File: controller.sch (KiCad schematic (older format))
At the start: 12 parts

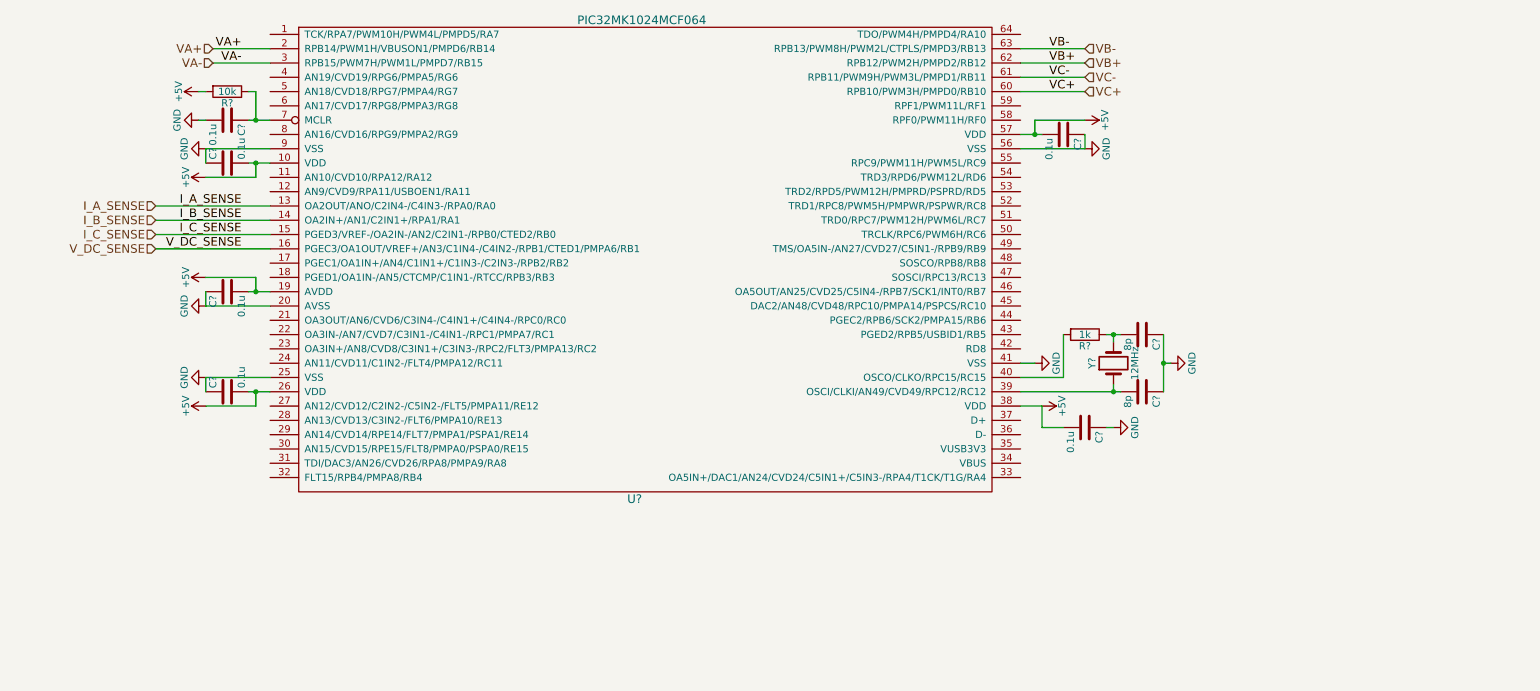
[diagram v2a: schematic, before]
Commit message: Implementing more faults and organizing.
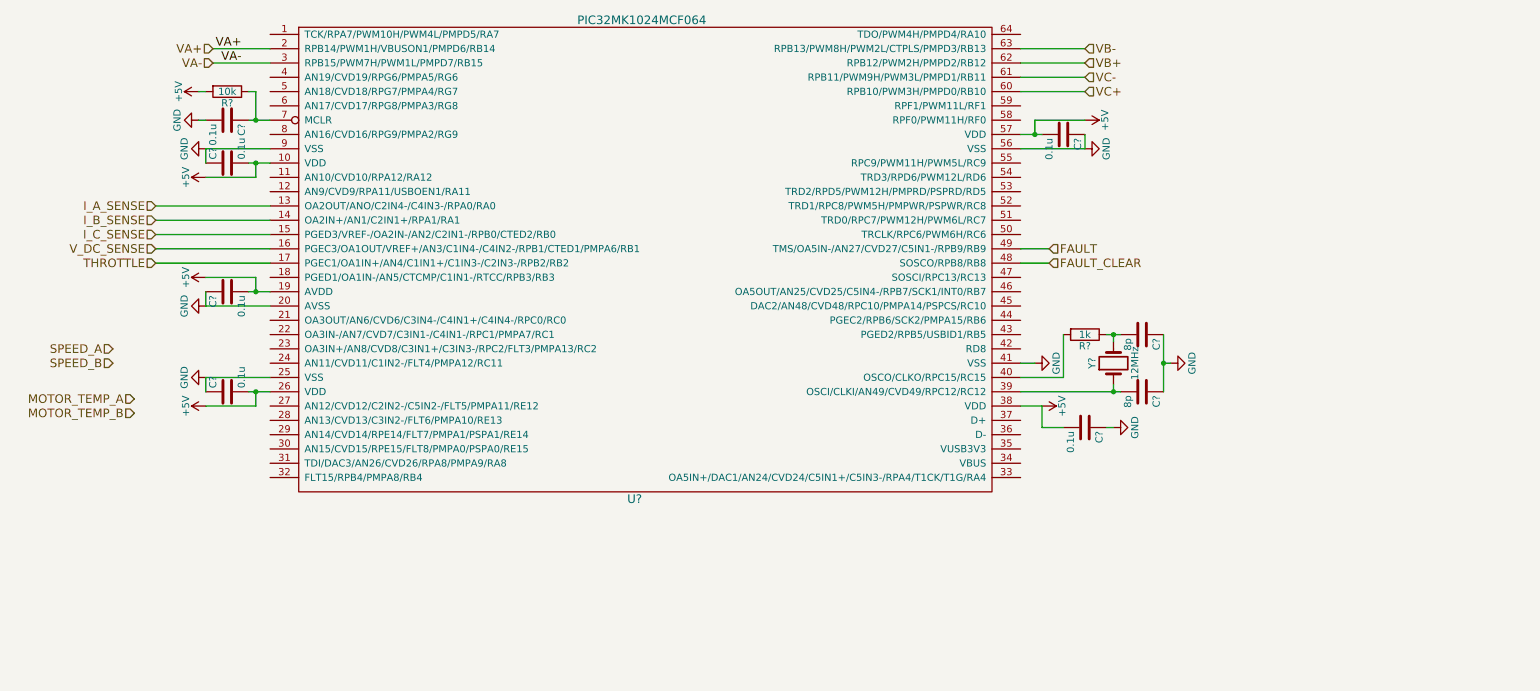
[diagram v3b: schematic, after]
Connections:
- net THROTTLE: now reaches U?.17 (PGEC1/OA1IN+/AN4/C1IN1+/C1IN3-/C2IN3-/RPB2/RB2)
- net FAULT_CLEAR: now reaches U?.48 (SOSCO/RPB8/RB8)
- net FAULT: now reaches U?.49 (TMS/OA5IN-/AN27/CVD27/C5IN1-/RPB9/RB9)
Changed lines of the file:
@@
 $Descr A4 11693 8268
 encoding utf-8
-Sheet 2 9
+Sheet 2 15
 Title ""
 Date ""
@@
 $EndComp
 $Comp
-L GND #PWR?
+L GND #PWR01
 U 1 1 5AEC2707
 P 8600 3350
-F 0 "#PWR?" H 8600 3100 50  0001 C CNN
+F 0 "#PWR01" H 8600 3100 50  0001 C CNN
 F 1 "GND" H 8600 3200 50  0000 C CNN
 F 2 "" H 8600 3350 50  0001 C CNN
@@
 $EndComp
 $Comp
-L GND #PWR?
+L GND #PWR02
 U 1 1 5AEC270D
 P 1850 1850
-F 0 "#PWR?" H 1850 1600 50  0001 C CNN
+F 0 "#PWR02" H 1850 1600 50  0001 C CNN
 F 1 "GND" H 1850 1700 50  0000 C CNN
 F 2 "" H 1850 1850 50  0001 C CNN
@@
 $EndComp
 $Comp
-L +5V #PWR?
+L +5V #PWR03
 U 1 1 5AEC271A
 P 1850 2050
-F 0 "#PWR?" H 1850 1900 50  0001 C CNN
+F 0 "#PWR03" H 1850 1900 50  0001 C CNN
 F 1 "+5V" H 1850 2190 50  0000 C CNN
 F 2 "" H 1850 2050 50  0001 C CNN
@@
 $EndComp
 $Comp
-L GND #PWR?
+L GND #PWR04
 U 1 1 5AEC2720
 P 1850 3450
-F 0 "#PWR?" H 1850 3200 50  0001 C CNN
+F 0 "#PWR04" H 1850 3200 50  0001 C CNN
 F 1 "GND" H 1850 3300 50  0000 C CNN
 F 2 "" H 1850 3450 50  0001 C CNN
@@
 $EndComp
 $Comp
-L +5V #PWR?
+L +5V #PWR05
 U 1 1 5AEC272D
 P 1850 3650
-F 0 "#PWR?" H 1850 3500 50  0001 C CNN
+F 0 "#PWR05" H 1850 3500 50  0001 C CNN
 F 1 "+5V" H 1850 3790 50  0000 C CNN
 F 2 "" H 1850 3650 50  0001 C CNN
@@
 $EndComp
 $Comp
-L GND #PWR?
+L GND #PWR06
 U 1 1 5AEC2733
 P 8000 1850
-F 0 "#PWR?" H 8000 1600 50  0001 C CNN
+F 0 "#PWR06" H 8000 1600 50  0001 C CNN
 F 1 "GND" H 8000 1700 50  0000 C CNN
 F 2 "" H 8000 1850 50  0001 C CNN
@@
 $EndComp
 $Comp
-L +5V #PWR?
+L +5V #PWR07
 U 1 1 5AEC2740
 P 8000 1650
-F 0 "#PWR?" H 8000 1500 50  0001 C CNN
+F 0 "#PWR07" H 8000 1500 50  0001 C CNN
 F 1 "+5V" H 8000 1790 50  0000 C CNN
 F 2 "" H 8000 1650 50  0001 C CNN
@@
 $EndComp
 $Comp
-L GND #PWR?
+L GND #PWR08
 U 1 1 5AEC2746
 P 1850 2950
-F 0 "#PWR?" H 1850 2700 50  0001 C CNN
+F 0 "#PWR08" H 1850 2700 50  0001 C CNN
 F 1 "GND" H 1850 2800 50  0000 C CNN
 F 2 "" H 1850 2950 50  0001 C CNN
@@
 $EndComp
 $Comp
-L +5V #PWR?
+L +5V #PWR09
 U 1 1 5AEC2753
 P 1850 2750
-F 0 "#PWR?" H 1850 2600 50  0001 C CNN
+F 0 "#PWR09" H 1850 2600 50  0001 C CNN
 F 1 "+5V" H 1850 2890 50  0000 C CNN
 F 2 "" H 1850 2750 50  0001 C CNN
@@
 $EndComp
 $Comp
-L GND #PWR?
+L GND #PWR010
 U 1 1 5AEC2759
 P 7650 3350
-F 0 "#PWR?" H 7650 3100 50  0001 C CNN
+F 0 "#PWR010" H 7650 3100 50  0001 C CNN
 F 1 "GND" H 7650 3200 50  0000 C CNN
 F 2 "" H 7650 3350 50  0001 C CNN
@@
 $EndComp
 $Comp
-L GND #PWR?
+L GND #PWR011
 U 1 1 5AEC275F
 P 8200 3800
-F 0 "#PWR?" H 8200 3550 50  0001 C CNN
+F 0 "#PWR011" H 8200 3550 50  0001 C CNN
 F 1 "GND" H 8200 3650 50  0000 C CNN
 F 2 "" H 8200 3800 50  0001 C CNN
@@
 $EndComp
 $Comp
-L +5V #PWR?
+L +5V #PWR012
 U 1 1 5AEC276C
 P 7700 3650
-F 0 "#PWR?" H 7700 3500 50  0001 C CNN
+F 0 "#PWR012" H 7700 3500 50  0001 C CNN
 F 1 "+5V" H 7700 3790 50  0000 C CNN
 F 2 "" H 7700 3650 50  0001 C CNN
@@
 $EndComp
 $Comp
-L GND #PWR?
+L GND #PWR013
 U 1 1 5AEC2780
 P 1800 1650
-F 0 "#PWR?" H 1800 1400 50  0001 C CNN
+F 0 "#PWR013" H 1800 1400 50  0001 C CNN
 F 1 "GND" H 1800 1500 50  0000 C CNN
 F 2 "" H 1800 1650 50  0001 C CNN
@@
 $EndComp
 $Comp
-L +5V #PWR?
+L +5V #PWR014
 U 1 1 5AEC2786
 P 1800 1450
-F 0 "#PWR?" H 1800 1300 50  0001 C CNN
+F 0 "#PWR014" H 1800 1300 50  0001 C CNN
 F 1 "+5V" H 1800 1590 50  0000 C CNN
 F 2 "" H 1800 1450 50  0001 C CNN
@@
 Wire Wire Line
 	1900 1250 2300 1250
-Text Label 7750 1250 0    60   ~ 0
-VB+
-Text Label 7750 1350 0    60   ~ 0
-VC-
-Text Label 7750 1450 0    60   ~ 0
-VC+
 Wire Wire Line
 	7550 1450 8000 1450
@@
 Wire Wire Line
 	7550 1250 8000 1250
-Text Label 7750 1150 0    60   ~ 0
-VB-
 Wire Wire Line
 	7550 1150 8000 1150
-Text Label 2100 2250 2    60   ~ 0
-I_A_SENSE
-Text Label 2100 2350 2    60   ~ 0
-I_B_SENSE
-Text Label 2100 2450 2    60   ~ 0
-I_C_SENSE
 Wire Wire Line
 	1500 2250 2300 2250
@@
 Wire Wire Line
 	1500 2450 2300 2450
-Text Label 2100 2550 2    60   ~ 0
-V_DC_SENSE
 Wire Wire Line
 	1500 2550 2300 2550
@@
 Text HLabel 1500 2550 0    60   Input ~ 0
 V_DC_SENSE
+Text HLabel 1500 2650 0    60   Input ~ 0
+THROTTLE
+Wire Wire Line
+	1500 2650 2300 2650
+Text HLabel 7750 2550 2    60   Input ~ 0
+FAULT
+Wire Wire Line
+	7750 2550 7550 2550
+Text HLabel 7750 2650 2    60   Input ~ 0
+FAULT_CLEAR
+Wire Wire Line
+	7750 2650 7550 2650
+Text HLabel 1200 3250 0    60   Input ~ 0
+SPEED_A
+Text HLabel 1200 3350 0    60   Input ~ 0
+SPEED_B
+Text HLabel 1350 3600 0    60   Input ~ 0
+MOTOR_TEMP_A
+Text HLabel 1350 3700 0    60   Input ~ 0
+MOTOR_TEMP_B
 $EndSCHEMATC

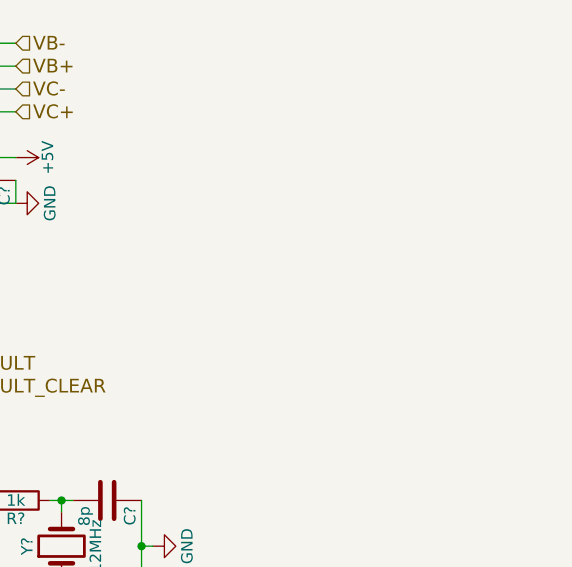
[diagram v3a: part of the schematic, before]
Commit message: Adding contactor placeholders.
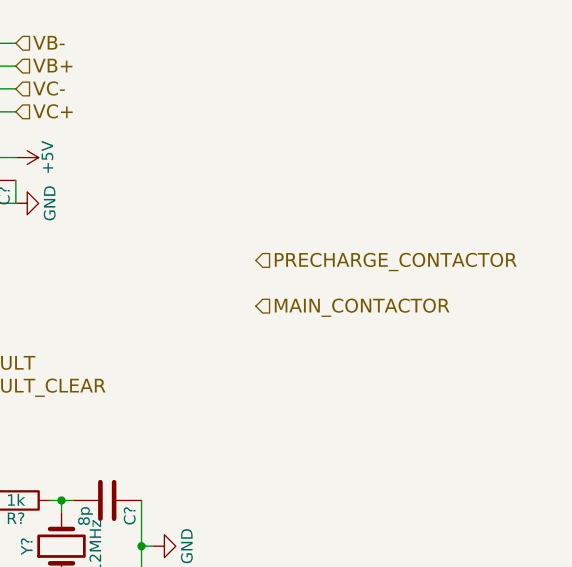
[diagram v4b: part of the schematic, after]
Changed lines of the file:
@@
 $Descr A4 11693 8268
 encoding utf-8
-Sheet 2 15
+Sheet 2 18
 Title ""
 Date ""
@@
 Text HLabel 1350 3700 0    60   Input ~ 0
 MOTOR_TEMP_B
+Text HLabel 9050 2100 2    60   Input ~ 0
+PRECHARGE_CONTACTOR
+Text HLabel 9050 2300 2    60   Input ~ 0
+MAIN_CONTACTOR
 $EndSCHEMATC

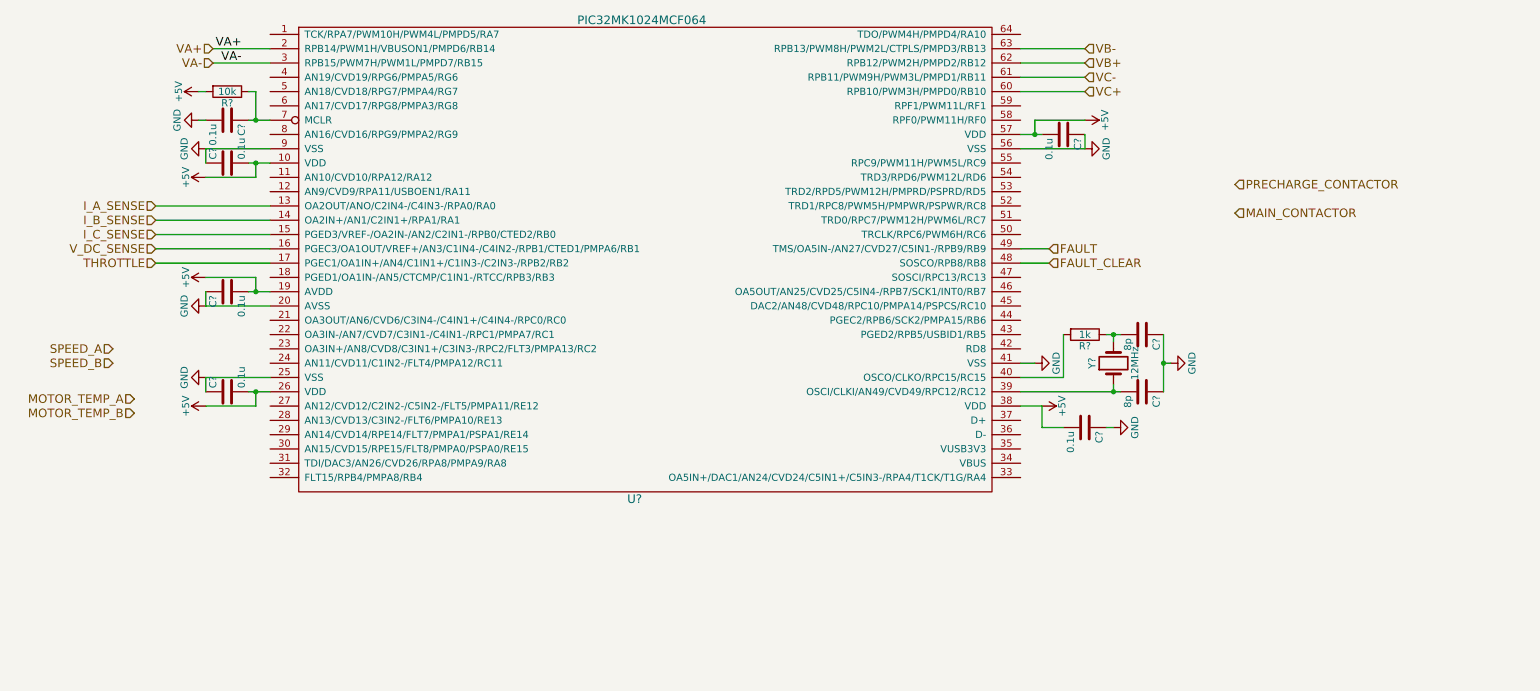
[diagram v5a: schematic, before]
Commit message: Connecting QEI inputs for speed encoder
Rewired other analog inputs to make QEI pins available.
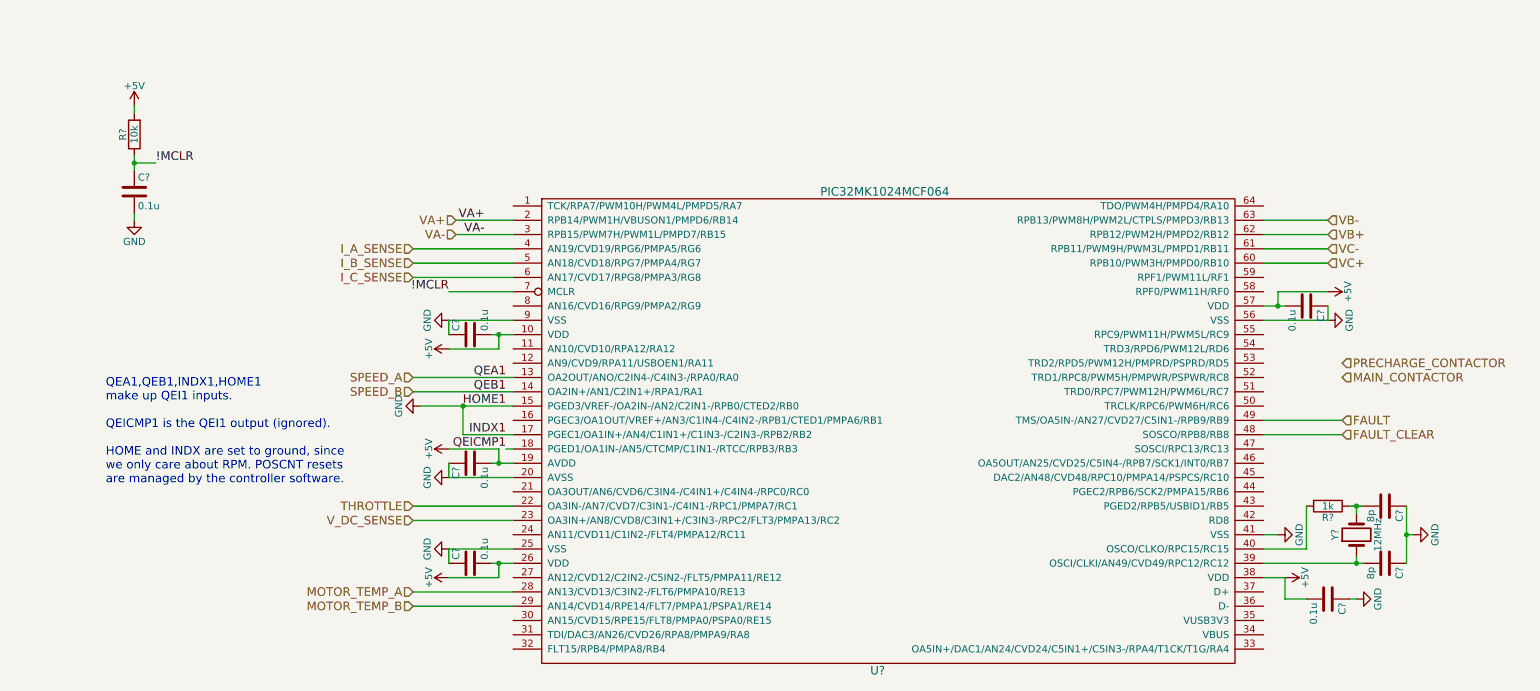
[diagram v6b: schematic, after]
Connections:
- net GND: now also U?.15 (PGED3/VREF-/OA2IN-/AN2/C2IN1-/RPB0/CTED2/RB0), U?.17 (PGEC1/OA1IN+/AN4/C1IN1+/C1IN3-/C2IN3-/RPB2/RB2)
- net I_A_SENSE: now also U?.4 (AN19/CVD19/RPG6/PMPA5/RG6); no longer U?.13 (OA2OUT/ANO/C2IN4-/C4IN3-/RPA0/RA0)
- net I_B_SENSE: now also U?.5 (AN18/CVD18/RPG7/PMPA4/RG7); no longer U?.14 (OA2IN+/AN1/C2IN1+/RPA1/RA1)
- net I_C_SENSE: now also U?.6 (AN17/CVD17/RPG8/PMPA3/RG8); no longer U?.15 (PGED3/VREF-/OA2IN-/AN2/C2IN1-/RPB0/CTED2/RB0)
- net MOTOR_TEMP_A: now also U?.28 (AN13/CVD13/C3IN2-/FLT6/PMPA10/RE13)
- net MOTOR_TEMP_B: now also U?.29 (AN14/CVD14/RPE14/FLT7/PMPA1/PSPA1/RE14)
- net SPEED_A: now also U?.13 (OA2OUT/ANO/C2IN4-/C4IN3-/RPA0/RA0)
- net SPEED_B: now also U?.14 (OA2IN+/AN1/C2IN1+/RPA1/RA1)
- net THROTTLE: now also U?.22 (OA3IN-/AN7/CVD7/C3IN1-/C4IN1-/RPC1/PMPA7/RC1); no longer U?.17 (PGEC1/OA1IN+/AN4/C1IN1+/C1IN3-/C2IN3-/RPB2/RB2)
- net V_DC_SENSE: now also U?.23 (OA3IN+/AN8/CVD8/C3IN1+/C3IN3-/RPC2/FLT3/PMPA13/RC2); no longer U?.16 (PGEC3/OA1OUT/VREF+/AN3/C1IN4-/C4IN2-/RPB1/CTED1/PMPA6/RB1)
- net QEICMP1: now reaches U?.18 (PGED1/OA1IN-/AN5/CTCMP/C1IN1-/RTCC/RPB3/RB3)
- net !MCLR: now reaches C?.1, R?.1, U?.7 (MCLR)
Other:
- note added: "QEA1,QEB1,INDX1,HOME1\nmake up QEI1 inputs.\n\nQEICMP1 is the QEI1 output (ignored).\n\nHOME and INDX are set to ground, since\nwe only care about RPM. POSCNT resets\nare managed by the controller software."
- moved on the sheet: C?, R?, U?, Y?

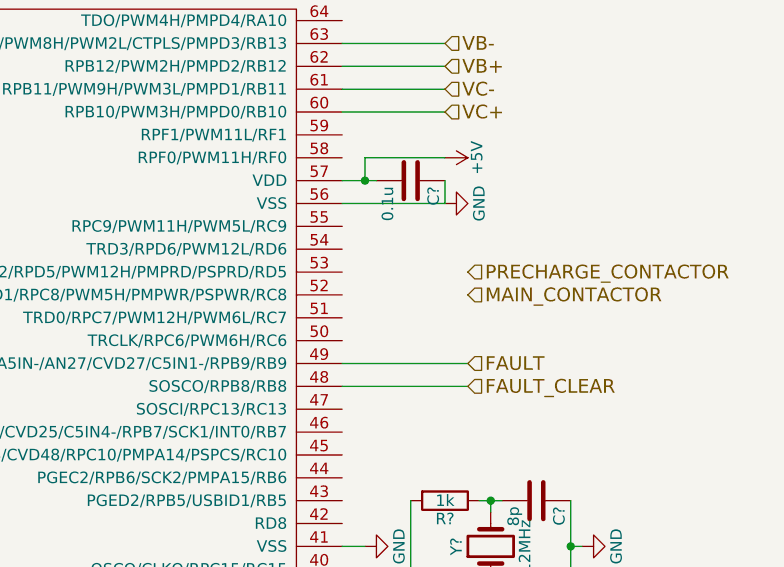
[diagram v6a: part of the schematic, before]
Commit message: Connect contactor signals.
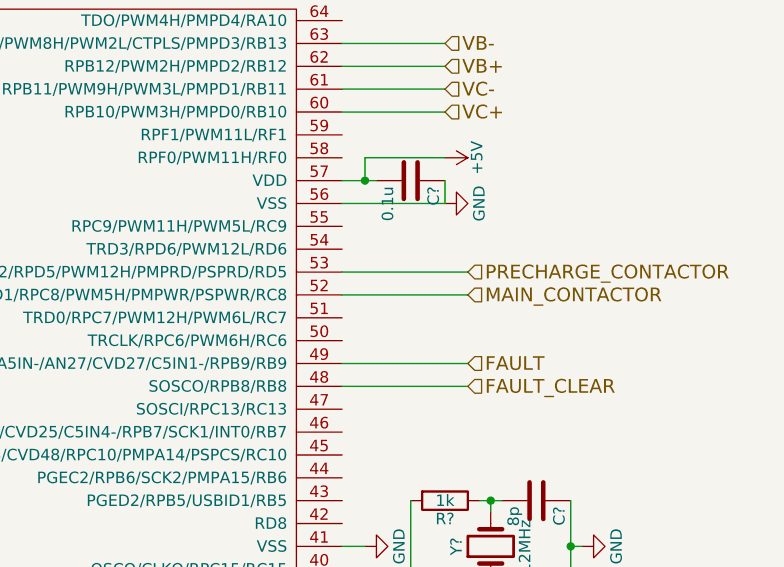
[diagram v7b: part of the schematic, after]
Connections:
- net MAIN_CONTACTOR: now also U?.52 (TRD1/RPC8/PWM5H/PMPWR/PSPWR/RC8)
- net PRECHARGE_CONTACTOR: now also U?.53 (TRD2/RPD5/PWM12H/PMPRD/PSPRD/RD5)
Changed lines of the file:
@@
 	1500 1950 1350 1950
 Connection ~ 1350 1950
+Wire Wire Line
+	9800 3350 9250 3350
+Wire Wire Line
+	9800 3450 9250 3450
 $EndSCHEMATC
